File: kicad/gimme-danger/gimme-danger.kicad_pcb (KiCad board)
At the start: 2 copper layers, 8.9 x 10.6 mm, 4 parts, among them U1 ESP32-S3-WROOM-1, U2 TPD6S300RUKR, U3 U261-241N-4BS2SS

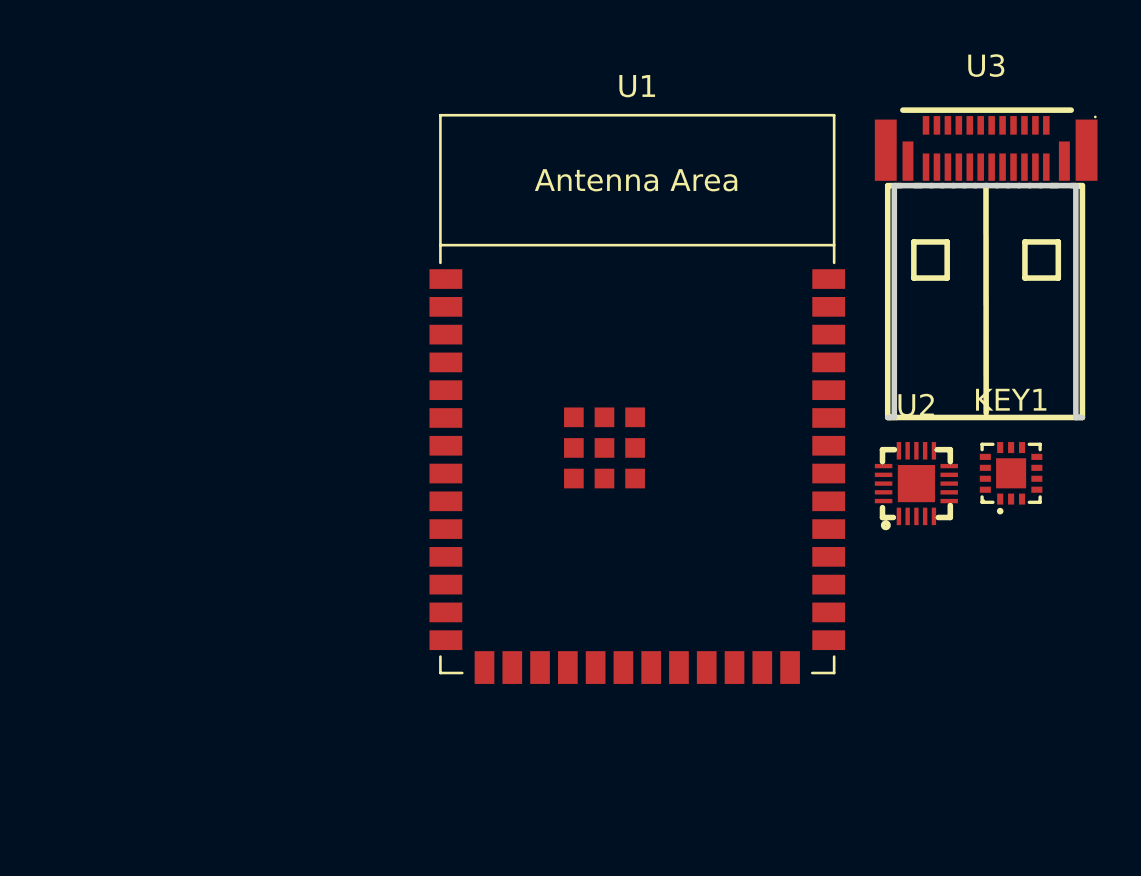
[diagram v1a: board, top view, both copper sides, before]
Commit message: Add NX20P5090 IC for switching
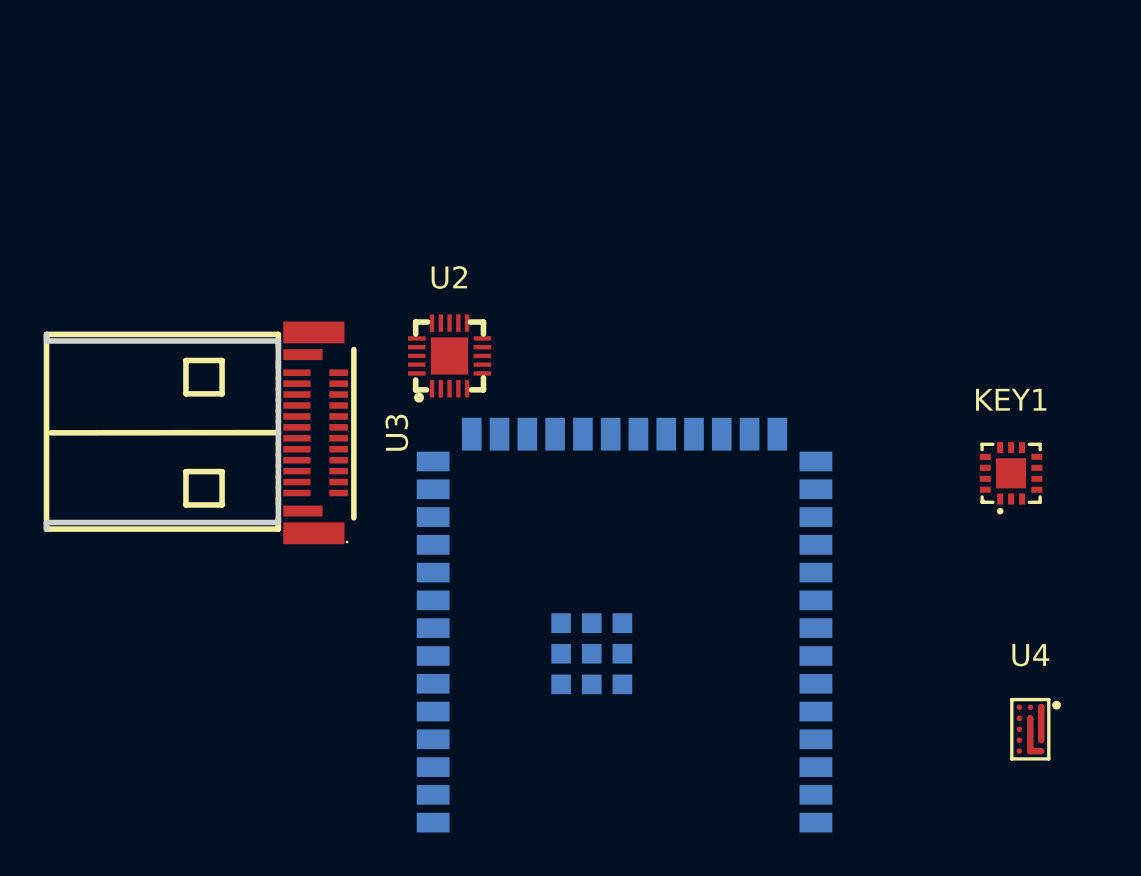
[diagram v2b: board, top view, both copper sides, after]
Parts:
- added U4: NX20P5090UKAZ, footprint:WLCSP-15_L2.6-W1.6-R3-C5-P0.50-TL_NXP, F.Cu at (95.2, 75.3)
- U1: moved to B.Cu
- moved U3 33.2 mm to (62.7, 61.8), turned to -90 degrees
- moved U2 22.1 mm to (68.7, 58.2)
- moved U1 8.35 mm to (76.7, 71.3)
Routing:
- net Net-(U4-VBUS-PadB2): track 0.00 -> 2.00 mm
- net Net-(U4-VINT-PadA1): track 0.00 -> 1.50 mm
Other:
- board size 8.9 x 10.6 mm -> 10.6 x 8.9 mm

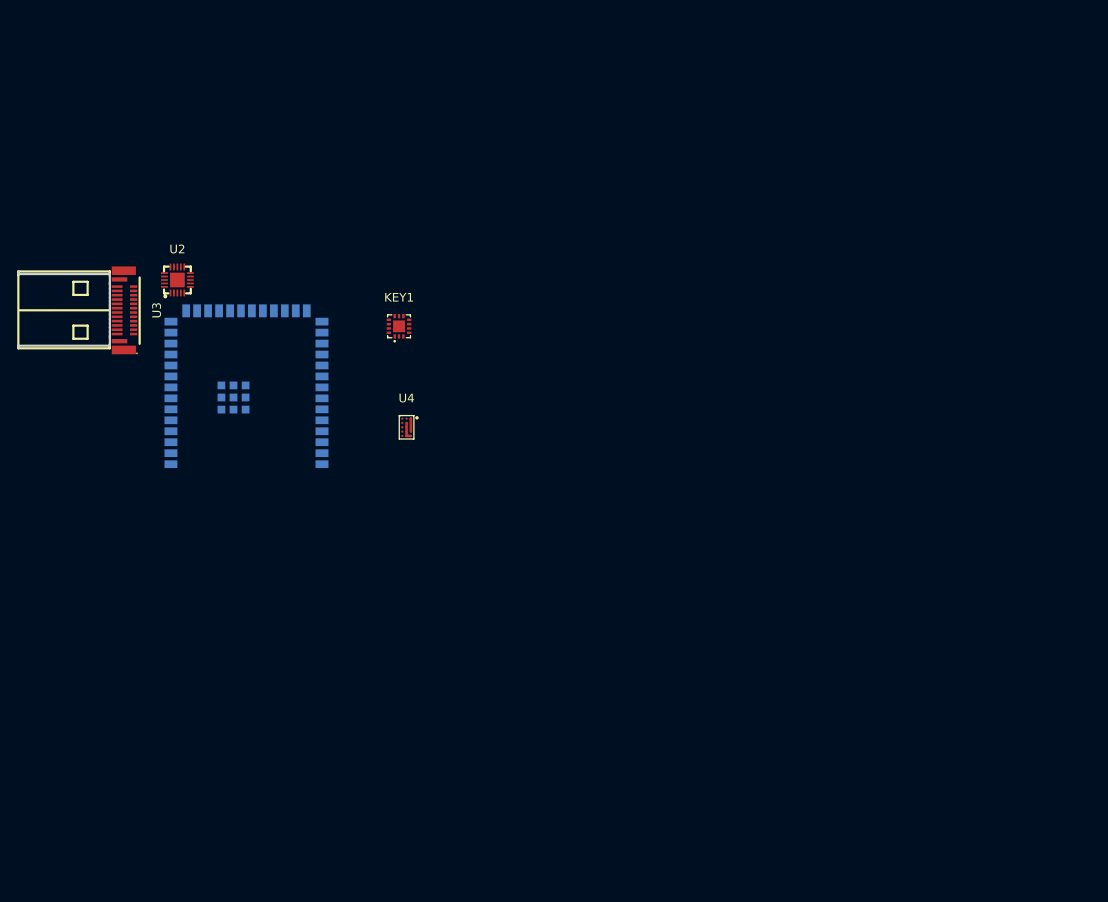
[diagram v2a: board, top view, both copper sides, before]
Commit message: First pass on schematics -- needs double checking, esp decoupling caps
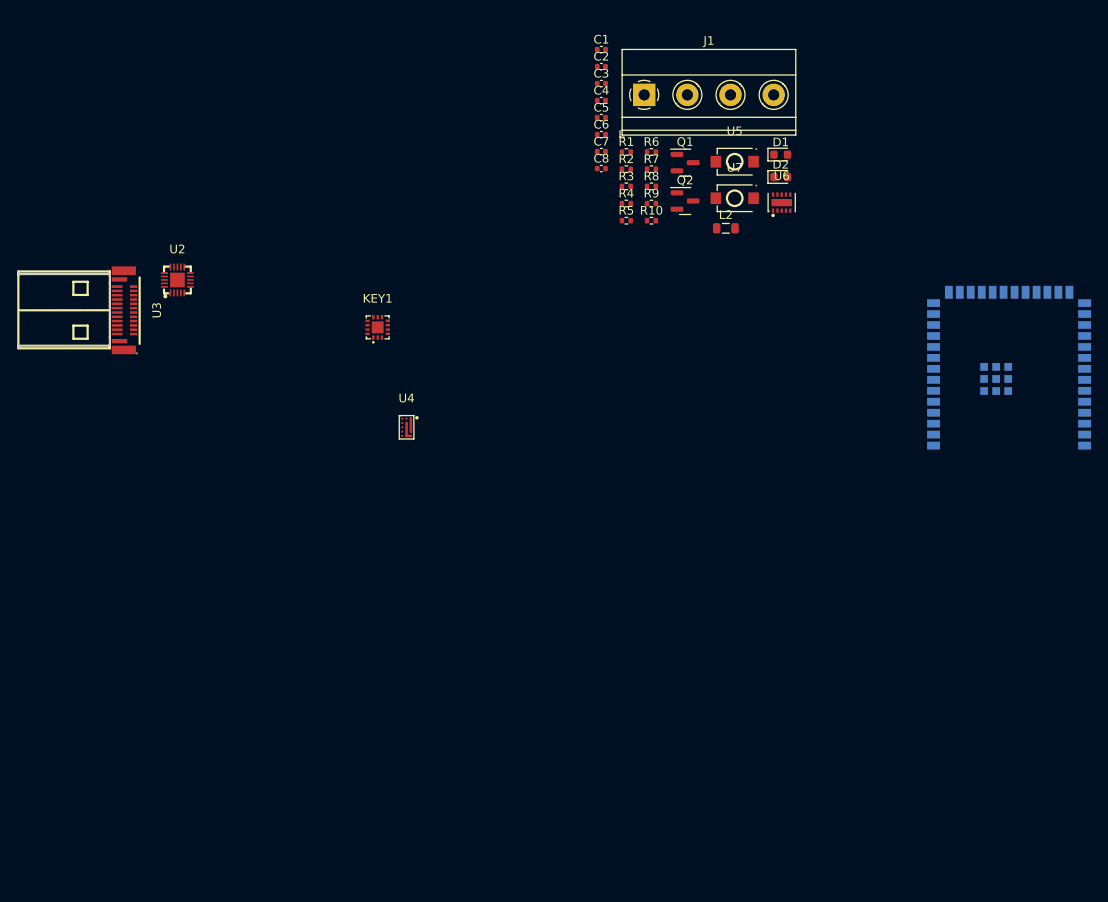
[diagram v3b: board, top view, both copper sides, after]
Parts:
- added C1: 10n, Capacitor_SMD:C_0402_1005Metric, F.Cu at (117.8, 31.5)
- added C2: 0.1u, Capacitor_SMD:C_0402_1005Metric, F.Cu at (117.8, 33.5)
- added C3: 22n, Capacitor_SMD:C_0402_1005Metric, F.Cu at (117.8, 35.5)
- added C4: 2.2n, Capacitor_SMD:C_0402_1005Metric, F.Cu at (117.8, 37.5)
- added C5: 0.1u, Capacitor_SMD:C_0402_1005Metric, F.Cu at (117.8, 39.4)
- added C6: 22n, Capacitor_SMD:C_0402_1005Metric, F.Cu at (117.8, 41.4)
- added C7: 0.1u, Capacitor_SMD:C_0402_1005Metric, F.Cu at (117.8, 43.4)
- added C8: 220p, Capacitor_SMD:C_0402_1005Metric, F.Cu at (117.8, 45.3)
- added D1: Red, LED_SMD:LED_0603_1608Metric, F.Cu at (138.6, 43.7)
- added D2: Green, LED_SMD:LED_0603_1608Metric, F.Cu at (138.6, 46.3)
- added J1: Screw_Terminal_01x04, TerminalBlock_Phoenix:TerminalBlock_Phoenix_MKDS-1,5-4_1x04_P5.00mm_Horizontal, F.Cu at (122.8, 36.8)
- added L2: 10uH, Inductor_SMD:L_0805_2012Metric, F.Cu at (132.2, 52.2)
- added Q1: AO3400A, Package_TO_SOT_SMD:SOT-23, F.Cu at (127.5, 44.6)
- added Q2: AO3400A, Package_TO_SOT_SMD:SOT-23, F.Cu at (127.5, 49.1)
- added R1: 10k, Resistor_SMD:R_0402_1005Metric, F.Cu at (120.7, 43.4)
- added R10: 100, Resistor_SMD:R_0402_1005Metric, F.Cu at (123.6, 51.4)
- added R2: 4k7, Resistor_SMD:R_0402_1005Metric, F.Cu at (120.7, 45.4)
- added R3: 4k7, Resistor_SMD:R_0402_1005Metric, F.Cu at (120.7, 47.4)
- added R4: 10k, Resistor_SMD:R_0402_1005Metric, F.Cu at (120.7, 49.4)
- added R5: 1k, Resistor_SMD:R_0402_1005Metric, F.Cu at (120.7, 51.4)
- added R6: 1k, Resistor_SMD:R_0402_1005Metric, F.Cu at (123.6, 43.4)
- added R7: 10k, Resistor_SMD:R_0402_1005Metric, F.Cu at (123.6, 45.4)
- added R8: 100k, Resistor_SMD:R_0402_1005Metric, F.Cu at (123.6, 47.4)
- added R9: 100, Resistor_SMD:R_0402_1005Metric, F.Cu at (123.6, 49.4)
- added U5: SKRKAEE020, footprint:SW-SMD_L3.9-W3.0-P4.45, F.Cu at (133.3, 44.5)
- added U6: TPS62177DQCR, footprint:WSON-10_L3.0-W2.0-P0.50-BL-EP, F.Cu at (138.7, 49.3)
- added U7: SKRKAEE020, footprint:SW-SMD_L3.9-W3.0-P4.45, F.Cu at (133.3, 48.8)
- moved U1 88.4 mm to (165.1, 69.2)
- moved KEY1 2.48 mm to (91.9, 63.7)
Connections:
- net Net-(U4-VINT-PadA1) renamed VINT
- KEY1 pad 10: unconnected-(KEY1-CC1-Pad10) -> CC1
- KEY1 pad 11: unconnected-(KEY1-CC1-Pad11) -> CC1
- KEY1 pad 12: unconnected-(KEY1-VCONN-Pad12) -> +3V3
- KEY1 pad 13: unconnected-(KEY1-VCONN-Pad13) -> +3V3
- KEY1 pad 15: unconnected-(KEY1-EP-Pad15) -> GND
- KEY1 pad 2: unconnected-(KEY1-VBUS-Pad2) -> VBUS
- KEY1 pad 3: unconnected-(KEY1-VDD-Pad3) -> +3V3
- KEY1 pad 4: unconnected-(KEY1-VDD-Pad4) -> +3V3
- KEY1 pad 5: unconnected-(KEY1-INT_N-Pad5) -> INT
- KEY1 pad 6: unconnected-(KEY1-SCL-Pad6) -> SCL
- KEY1 pad 7: unconnected-(KEY1-SDA-Pad7) -> SDA
- KEY1 pad 8: unconnected-(KEY1-GND-Pad8) -> GND
- KEY1 pad 9: unconnected-(KEY1-GND-Pad9) -> GND
- U1 pad 1: Net-(U1-GND-Pad1) -> GND
- U1 pad 10: unconnected-(U1-GPIO17/U1TXD/ADC2_CH6-Pad10) -> Net-(U1-GPIO17/U1TXD/ADC2_CH6)
- U1 pad 11: unconnected-(U1-GPIO18/U1RXD/ADC2_CH7/CLK_OUT3-Pad11) -> Net-(U1-GPIO18/U1RXD/ADC2_CH7/CLK_OUT3)
- U1 pad 12: unconnected-(U1-GPIO8/TOUCH8/ADC1_CH7/SUBSPICS1-Pad12) -> SDA
- U1 pad 13: unconnected-(U1-GPIO19/U1RTS/ADC2_CH8/CLK_OUT2/USB_D--Pad13) -> D-
- U1 pad 14: unconnected-(U1-GPIO20/U1CTS/ADC2_CH9/CLK_OUT1/USB_D+-Pad14) -> D+
- U1 pad 17: unconnected-(U1-GPIO9/TOUCH9/ADC1_CH8/FSPIHD/SUBSPIHD-Pad17) -> SCL
- U1 pad 18: unconnected-(U1-GPIO10/TOUCH10/ADC1_CH9/FSPICS0/FSPIIO4/SUBSPICS0-Pad18) -> INT
- U1 pad 2: unconnected-(U1-3V3-Pad2) -> +3V3
- U1 pad 21: unconnected-(U1-GPIO13/TOUCH13/ADC2_CH2/FSPIQ/FSPIIO7/SUBSPIQ-Pad21) -> LED_GREEN
- U1 pad 22: unconnected-(U1-GPIO14/TOUCH14/ADC2_CH3/FSPIWP/FSPIDQS/SUBSPIWP-Pad22) -> LED_RED
- U1 pad 27: unconnected-(U1-GPIO0/BOOT-Pad27) -> Net-(U1-GPIO0/BOOT)
- U1 pad 3: unconnected-(U1-EN-Pad3) -> Net-(U1-EN)
- U1 pad 36: unconnected-(U1-U0RXD/GPIO44/CLK_OUT2-Pad36) -> RX
- U1 pad 37: unconnected-(U1-U0TXD/GPIO43/CLK_OUT1-Pad37) -> TX
- U1 pad 38: unconnected-(U1-GPIO2/TOUCH2/ADC1_CH1-Pad38) -> VMON
- U1 pad 40: Net-(U1-GND-Pad1) -> GND
- U1 pad 41: Net-(U1-GND-Pad1) -> GND
- U2 pad 1: unconnected-(U2-C_SBU1-Pad1) -> C_SBU1
- U2 pad 10: unconnected-(U2-VPWR-Pad10) -> +3V3
- U2 pad 12: unconnected-(U2-CC1-Pad12) -> CC1
- U2 pad 13: unconnected-(U2-GND-Pad13) -> GND
- U2 pad 18: unconnected-(U2-GND-Pad18) -> GND
- U2 pad 19: unconnected-(U2-D2-Pad19) -> D+
- U2 pad 2: unconnected-(U2-C_SBU2-Pad2) -> C_SBU2
- U2 pad 20: unconnected-(U2-D1-Pad20) -> D-
- U2 pad 21: unconnected-(U2-EP-Pad21) -> GND
- U2 pad 3: unconnected-(U2-VBIAS-Pad3) -> Net-(U2-VBIAS)
- U2 pad 4: unconnected-(U2-C_CC1-Pad4) -> C_CC1
- U2 pad 8: unconnected-(U2-GND-Pad8) -> GND
- U3 pad 25: unconnected-(U3-GND-Pad25) -> GND
- U3 pad 26: unconnected-(U3-GND-Pad26) -> GND
- U3 pad A1: unconnected-(U3-GND-PadA1) -> GND
- U3 pad A12: unconnected-(U3-GND-PadA12) -> GND
- U3 pad A4: unconnected-(U3-VBUS-PadA4) -> VBUS
- U3 pad A5: unconnected-(U3-CC-PadA5) -> C_CC1
- U3 pad A6: unconnected-(U3-D+-PadA6) -> D+
- U3 pad A7: unconnected-(U3-D--PadA7) -> D-
- U3 pad A8: unconnected-(U3-SBU1-PadA8) -> C_SBU1
- U3 pad A9: unconnected-(U3-VBUS-PadA9) -> VBUS
- U3 pad B1: unconnected-(U3-GND-PadB1) -> GND
- U3 pad B12: unconnected-(U3-GND-PadB12) -> GND
- U3 pad B4: unconnected-(U3-VBUS-PadB4) -> VBUS
- U3 pad B8: unconnected-(U3-SBU2-PadB8) -> C_SBU2
- U3 pad B9: unconnected-(U3-VBUS-PadB9) -> VBUS
- U4 pad A3: unconnected-(U4-EN#-PadA3) -> Net-(JP1-A)
- U4 pad B2: Net-(U4-VBUS-PadB2) -> VBUS
- U4 pad B3: unconnected-(U4-OVLO-PadB3) -> GND
- U4 pad C2: Net-(U4-VBUS-PadB2) -> VBUS
- U4 pad C3: unconnected-(U4-GND-PadC3) -> GND
- U4 pad D2: Net-(U4-VBUS-PadB2) -> VBUS
- U4 pad D3: unconnected-(U4-GND-PadD3) -> GND
- U4 pad E1: Net-(U4-VBUS-PadB2) -> VBUS
- U4 pad E2: Net-(U4-VBUS-PadB2) -> VBUS
- U4 pad E3: unconnected-(U4-GND-PadE3) -> GND
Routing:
- net VBUS: track 0.00 -> 2.00 mm
- net Net-(U4-VBUS-PadB2): track 2.00 -> 0.00 mm

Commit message: Changed to more capable DC-DC converter (up to 1.2A)
Worst case: ESP32-S3 500 mA + FUSB302 500 mA
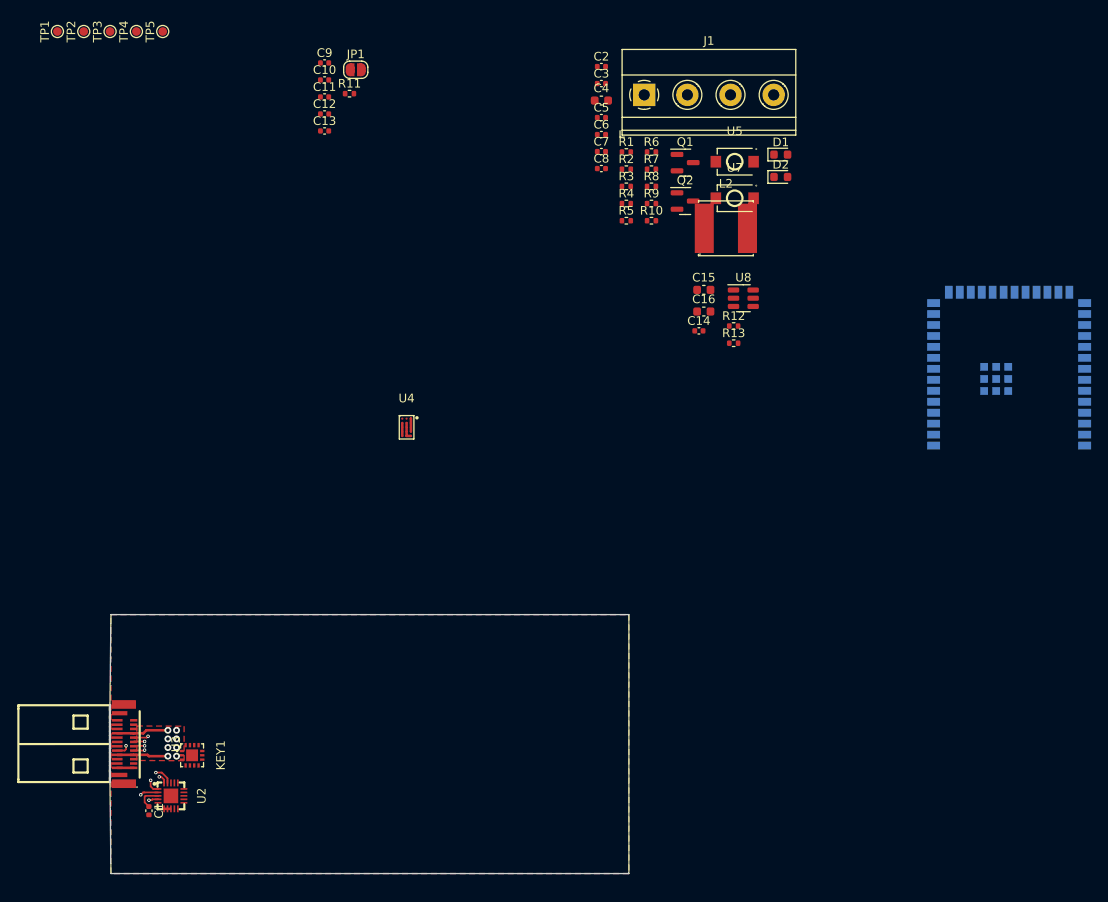
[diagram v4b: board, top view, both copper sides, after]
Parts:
- removed U6: TPS62177DQCR, footprint:WSON-10_L3.0-W2.0-P0.50-BL-EP
- added C10: 1u, Capacitor_SMD:C_0402_1005Metric, F.Cu at (85.8, 35.1)
- added C11: 1u, Capacitor_SMD:C_0402_1005Metric, F.Cu at (85.8, 37.0)
- added C12: 1u, Capacitor_SMD:C_0402_1005Metric, F.Cu at (85.8, 39.0)
- added C13: 0.1u, Capacitor_SMD:C_0402_1005Metric, F.Cu at (85.8, 41.0)
- added C14: 0.1u, Capacitor_SMD:C_0402_1005Metric, F.Cu at (129.1, 64.1)
- added C15: 10u, Capacitor_SMD:C_0603_1608Metric, F.Cu at (129.7, 59.4)
- added C16: 10u, Capacitor_SMD:C_0603_1608Metric, F.Cu at (129.7, 61.9)
- added C9: 1u, Capacitor_SMD:C_0402_1005Metric, F.Cu at (85.8, 33.1)
- added JP1: ~, Jumper:SolderJumper-2_P1.3mm_Open_RoundedPad1.0x1.5mm, F.Cu at (89.4, 33.9)
- added R11: 4k7, Resistor_SMD:R_0402_1005Metric, F.Cu at (88.6, 36.6)
- added R12: 100k, Resistor_SMD:R_0402_1005Metric, F.Cu at (133.1, 63.6)
- added R13: 100k, Resistor_SMD:R_0402_1005Metric, F.Cu at (133.1, 65.6)
- added TP1: 3v3, TestPoint:TestPoint_Pad_D1.0mm, F.Cu at (54.8, 29.4)
- added TP2: 3v3, TestPoint:TestPoint_Pad_D1.0mm, F.Cu at (57.9, 29.4)
- added TP3: 3v3, TestPoint:TestPoint_Pad_D1.0mm, F.Cu at (60.9, 29.4)
- added TP4: 3v3, TestPoint:TestPoint_Pad_D1.0mm, F.Cu at (64.0, 29.4)
- added TP5: 3v3, TestPoint:TestPoint_Pad_D1.0mm, F.Cu at (67.0, 29.4)
- added U8: TPS54302, Package_TO_SOT_SMD:SOT-23-6, F.Cu at (134.3, 60.4)
- C1: value 10n -> 100n
- C3: value 22n -> 0.1u
- C4: value 2.2n -> 10u; footprint Capacitor_SMD:C_0402_1005Metric -> Capacitor_SMD:C_0603_1608Metric
- L2: value 10uH -> YNR6045-470M; footprint Inductor_SMD:L_0805_2012Metric -> footprint:IND-SMD_L6.0-W6.0
- moved C1 102.6 mm to (65.4, 119.7), turned to -90 degrees
- moved U2 59.8 mm to (68.0, 118.0), turned to -90 degrees
- moved KEY1 54.0 mm to (70.4, 113.3), turned to -90 degrees
- moved U3 50.3 mm to (62.7, 112.0)
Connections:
- C3 pad 1: +3V3 -> VBUS
- L2 pad 1: +3V3 -> Net-(U8-SW)
- L2 pad 2: Net-(U6-SW) -> +3V3
- U1 pad 20: unconnected-(U1-GPIO12/TOUCH12/ADC2_CH1/FSPICLK/FSPIIO6/SUBSPICLK-Pad20) -> LOAD_EN#
- U2 pad 16: unconnected-(U2-N.C.-Pad16) -> GND
- U2 pad 17: unconnected-(U2-N.C.-Pad17) -> GND
- U2 pad 6: unconnected-(U2-RPD_G2-Pad6) -> GND
- U2 pad 7: unconnected-(U2-RPD_G1-Pad7) -> GND
- U4 pad A3: Net-(JP1-A) (its old number) -> LOAD_EN#
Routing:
- net VBUS: track 2.00 -> 14.6 mm, vias 0 -> 8
- net C_SBU1: track 0.00 -> 10.8 mm, vias 0 -> 2
- net C_SBU2: track 0.00 -> 10.4 mm, vias 0 -> 2
- net C_CC1: track 0.00 -> 8.28 mm, vias 0 -> 2
- net D-: track 0.00 -> 7.47 mm, vias 0 -> 2
- net D+: track 0.00 -> 7.33 mm, vias 0 -> 2
- net GND: track 0.00 -> 4.16 mm
- net Net-(U2-VBIAS): track 0.00 -> 2.94 mm
- added copper zone on In2.Cu, net +3V3
- added copper zone on B.Cu, net GND
- added copper zone on F.Cu, net GND
- added copper zone on F.Cu, net VBUS
- added copper zone on In1.Cu, net VBUS
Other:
- board size 10.6 x 8.9 mm -> 60.1 x 30 mm
- copper layers 2 -> 4
